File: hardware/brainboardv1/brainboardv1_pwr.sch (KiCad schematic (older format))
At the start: 3 parts

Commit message: Nearly finished v1 sch & brd, await final check
Fixed errors from Rev 0, added MPU-6050 accelerometer/gyro for head
motion tracking, switched to +/-2.5V analog supply, added 2 bipolar
analog inputs for EOG tracking, added daisy-chain capability
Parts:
- removed C?: 0.1uF, ~, symbol C
- removed P?: 5VA, ~, symbol TST
- removed U?: TPS73150, ~, symbol TPS73150
- added C36, C39, C43, C48: 10uF, ~, symbol C
- added C37, C38, C40, C41, C46: 1uF, ~, symbol C
- added C42, C47: 0.01uF, ~, symbol C
- added C44, C49: 2.2uF, ~, symbol C
- added C45: 0.1uF, ~, symbol C
- added P6: -3V3, ~, symbol TST
- added P8: +2V5, ~, symbol TST
- added P9: -2V5, ~, symbol TST
- added U10: TPS60403, ~, symbol TPS60403
- added U11: TPS73225, ~, symbol TPS73225
- added U12: TPS72325, ~, symbol TPS72325
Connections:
- net labels added: +2.5V, +3.3V, -2.5V, -3.3V, AGND, DGND
- net labels removed: +5VA, +5VD, GNDPWR
- wire segments 9 -> 48
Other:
- note removed: "Rev. 0 is meant for demonstration of basic signal acquisition capabilities\nand does not use battery power. +5VD is the VCC_5V supply from the\nBeagleBone. The TPS73150 is used for post-regulation."

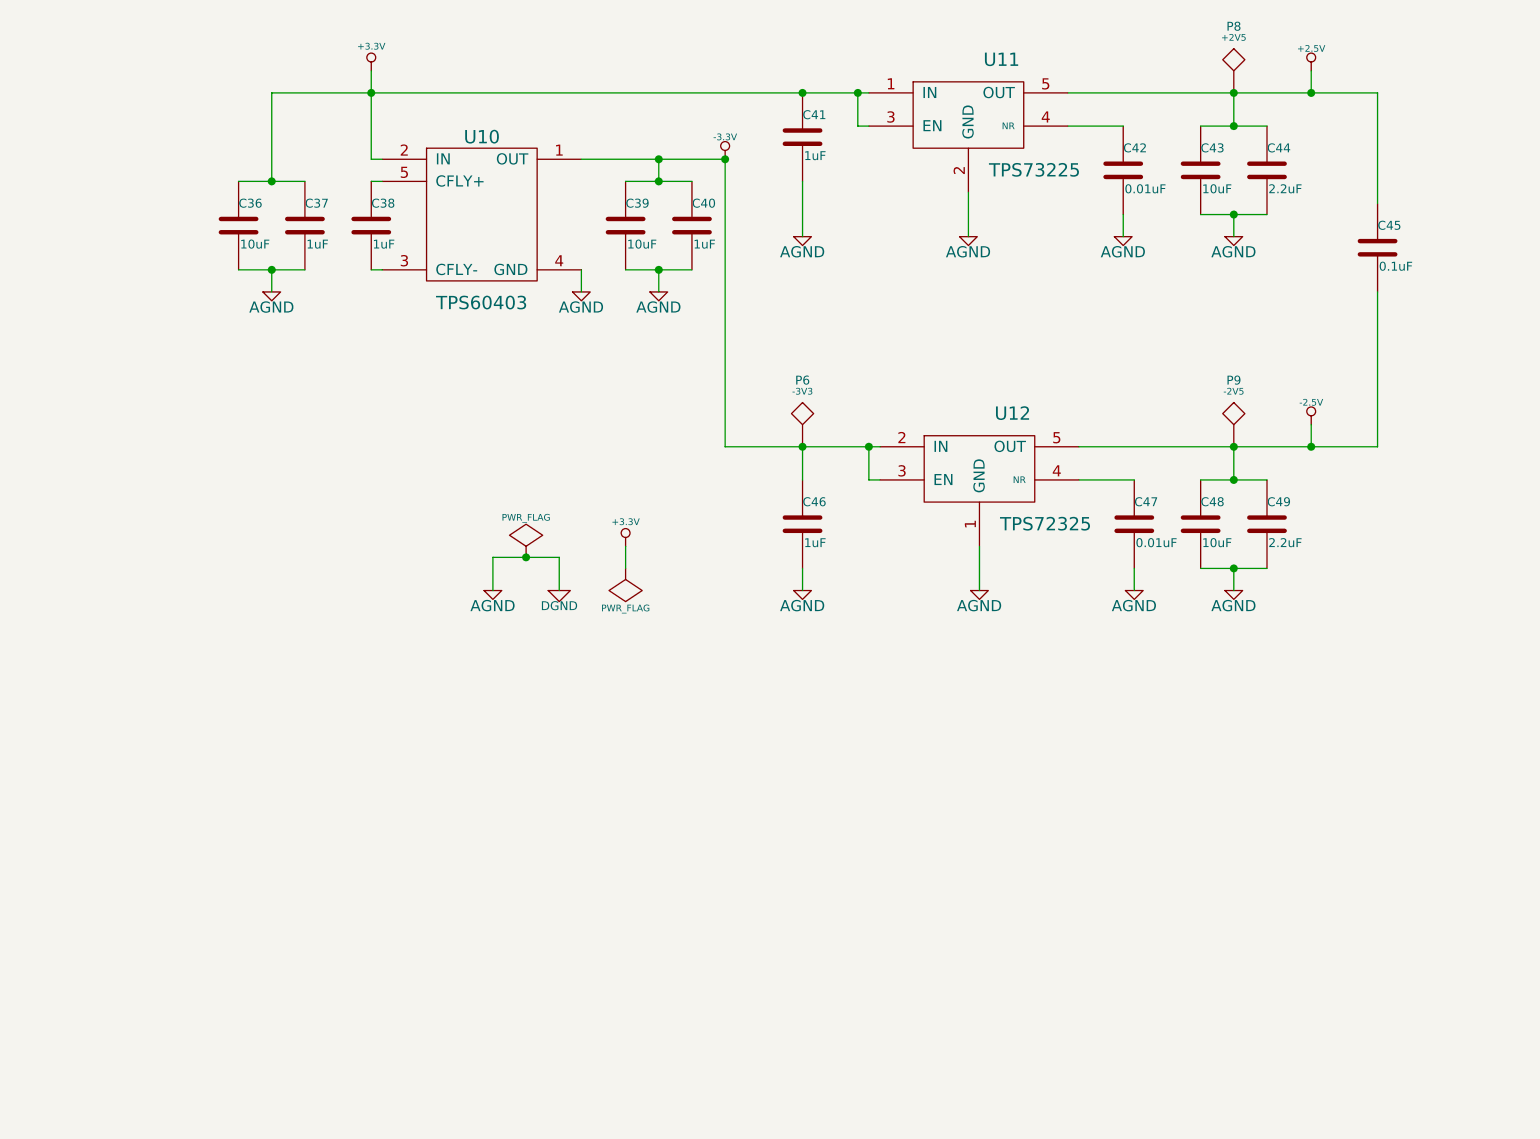
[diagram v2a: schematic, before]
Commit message: More battery changes
Added power-down logic to battery board (currently faulty, need
revision); added fuel gauge, 2-pin JST, and BBB battery connector to
Brainboard R1.
TODO: Fix power-down logic (suggest dedicated power-button supervisor
like STM660x), add isolation so board can be safely plugged in to charge
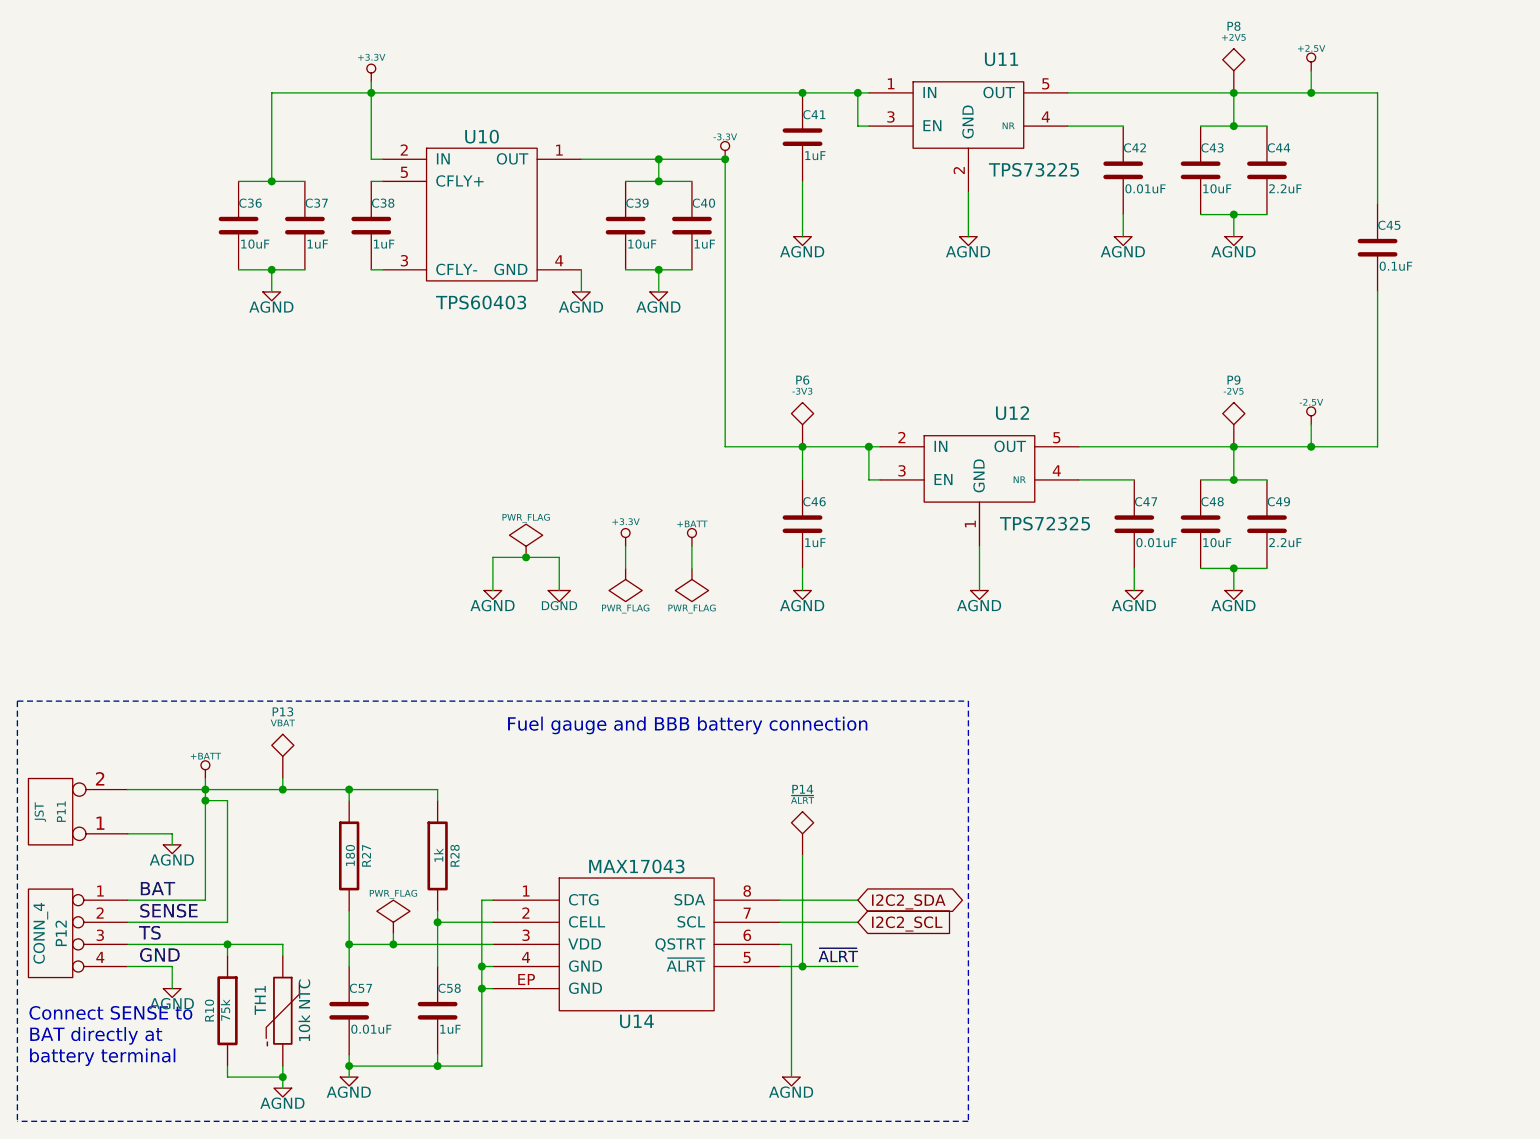
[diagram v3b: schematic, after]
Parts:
- added C57: 0.01uF, ~, symbol C
- added C58: 1uF, ~, symbol C
- added P11: JST, ~, symbol CONN_2
- added P12: CONN_4, ~, symbol CONN_4
- added P13: VBAT, ~, symbol TST
- added P14: ~ALRT, ~, symbol TST
- added R10: 75k, ~, symbol R
- added R27: 180, ~, symbol R
- added R28: 1k, ~, symbol R
- added TH1: 10k NTC, ~, symbol THERMISTOR
- added U14: MAX17043, ~, symbol MAX17043
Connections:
- net AGND: now also C57.2, C58.2, P11.1 (P1), P12.4 (P4), R10.2, TH1.2, U14.1 (CTG), U14.4 (GND), U14.6 (QSTRT), U14.EP (GND)
- new net: C58.1, R28.2, U14.2 (CELL)
- new net: C57.1, R27.2, U14.3 (VDD)
- new net +BATT: P11.2 (PM), P12.1 (P1), P12.2 (P2), P13.1, R27.1, R28.1
- new net I2C2_SCL: U14.7 (SCL)
- new net I2C2_SDA: U14.8 (SDA)
- new net TS: P12.3 (P3), R10.1, TH1.1
- new net ~ALRT: P14.1, U14.5 (~ALRT)
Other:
- note added: "Connect SENSE to\nBAT directly at\nbattery terminal"
- note added: "Fuel gauge and BBB battery connection"
